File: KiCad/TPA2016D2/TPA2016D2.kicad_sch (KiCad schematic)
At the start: 20 parts, among them IC1 TPA2016D2QFN, J1 TERMBLOCK_1X2, J2 TERMBLOCK_1X2

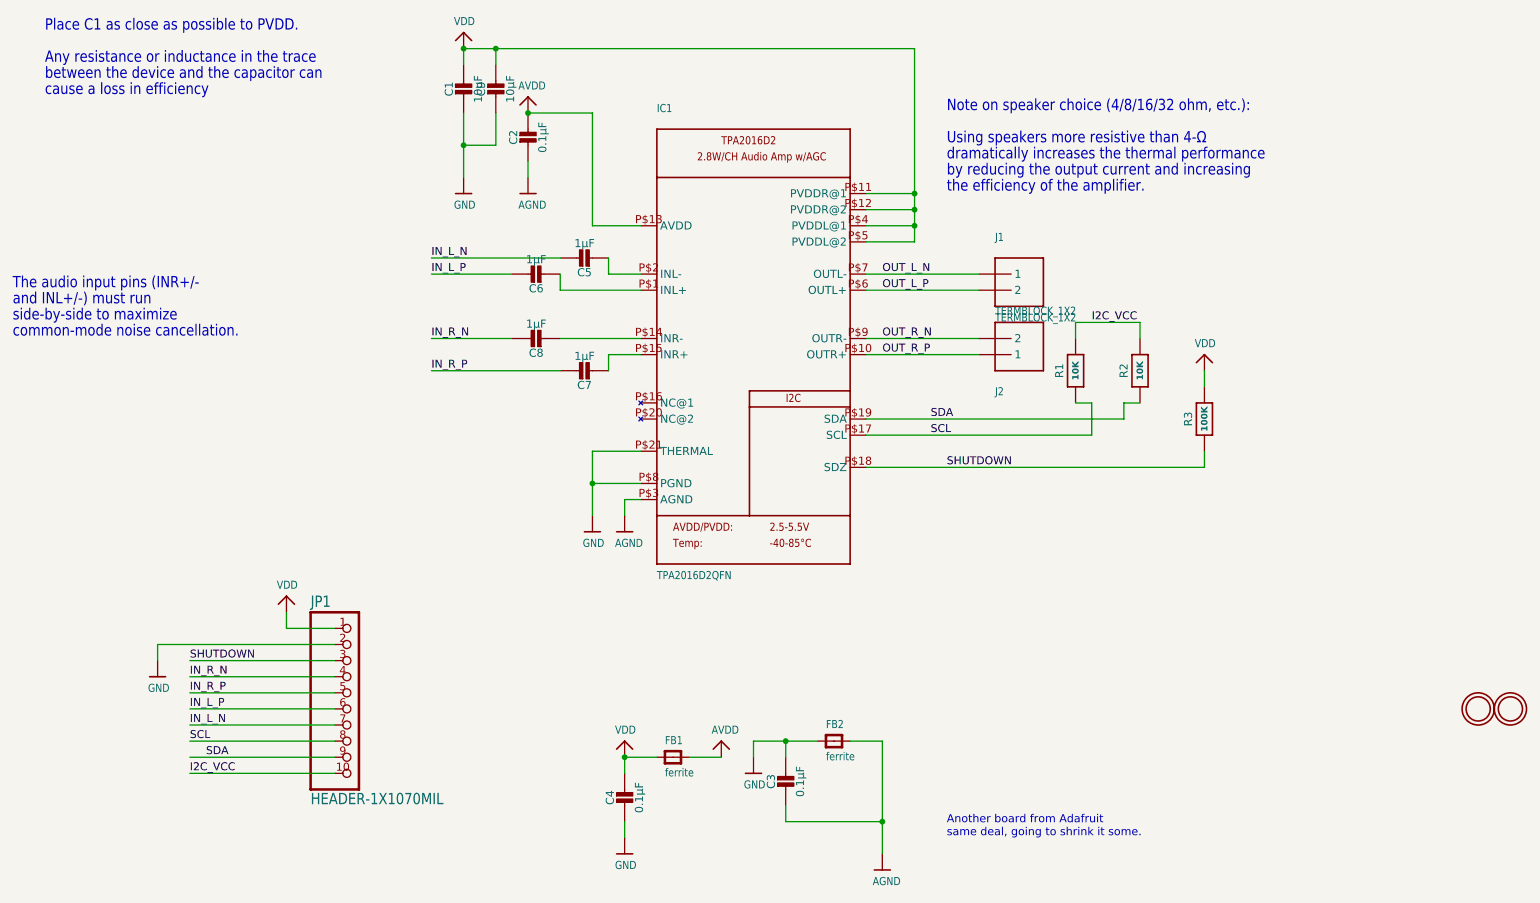
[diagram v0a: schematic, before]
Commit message: converted TPA2016D2 schematic to kicad symbols
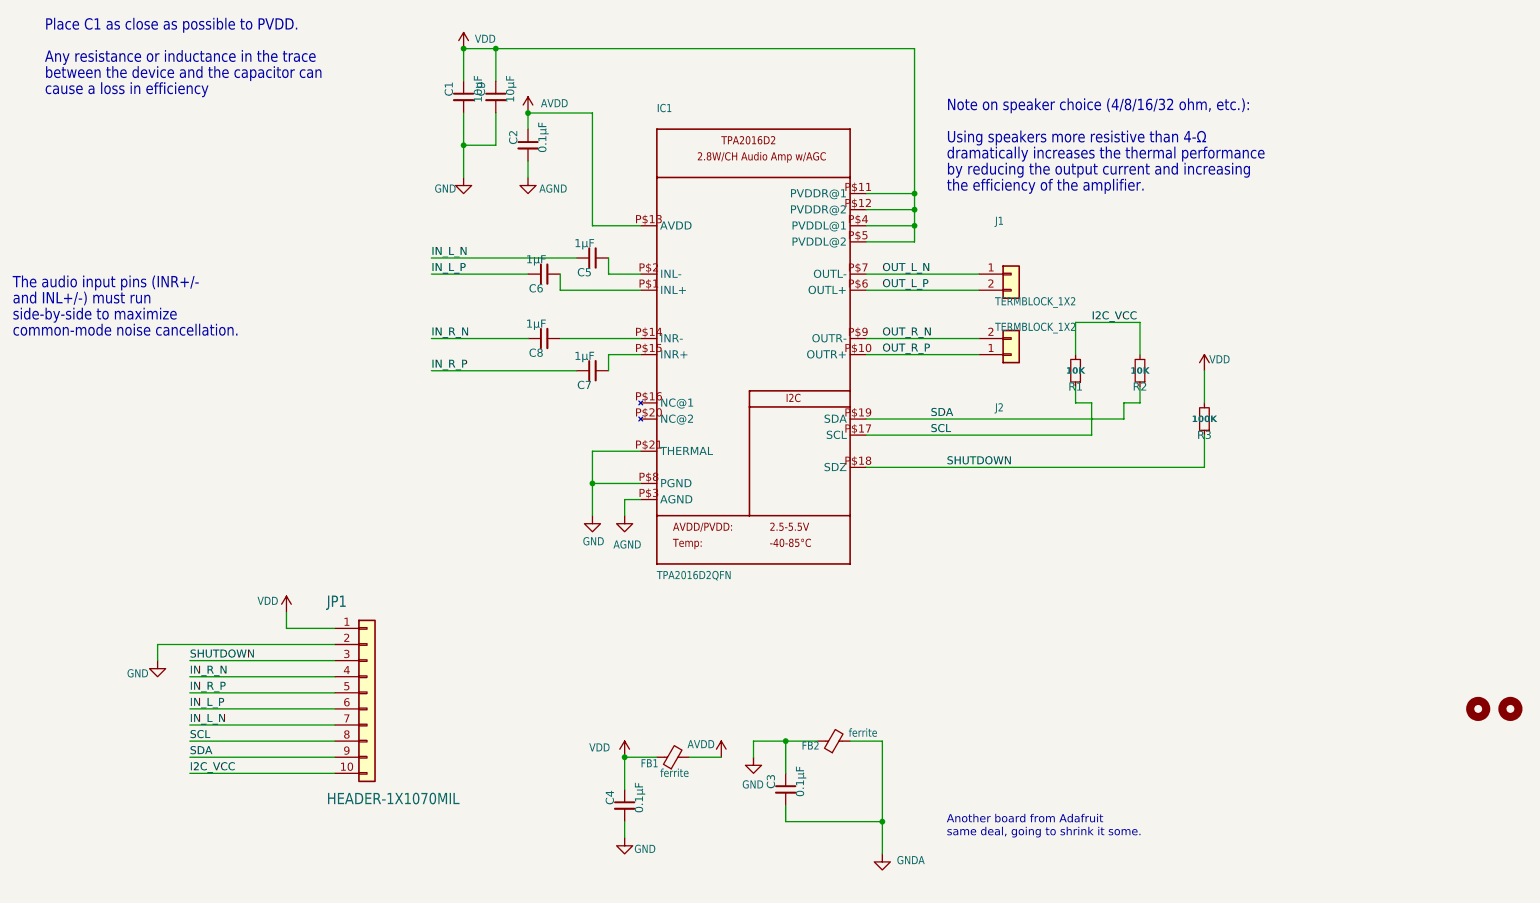
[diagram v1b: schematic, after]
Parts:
- C1, C2, C3, C4, C5, C6, C7, C8, C9: symbol TPA2016D2-eagle-import:CAP_CERAMIC0805-NOOUTLINE -> Device:C_Small
- FB1, FB2: symbol TPA2016D2-eagle-import:FERRITE_0805MP -> Device:FerriteBead_Small
- J1, J2: footprint TERMBLOCK_1X2-3.5MM -> Connector_PinHeader_2.54mm:PinHeader_1x02_P2.54mm_Vertical; symbol TPA2016D2-eagle-import:TERMBLOCK_1X2 -> Connector_Generic:Conn_01x02
- JP1: symbol TPA2016D2-eagle-import:HEADER-1X1070MIL -> Connector_Generic:Conn_01x10
- R1, R2, R3: symbol TPA2016D2-eagle-import:RESISTOR0805_NOOUTLINE -> Device:R_Small
- U$20, U$21: symbol TPA2016D2-eagle-import:MOUNTINGHOLE2.5_THICK -> Mechanical:MountingHole
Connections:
- net AGND renamed GNDA
- net AVDD renamed VDDA
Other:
- moved on the sheet: J1, J2
